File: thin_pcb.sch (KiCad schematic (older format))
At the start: 149 parts, among them J01 Conn_01x02, J02 Conn_01x02, J04 Conn_01x02, J06 Conn_01x02, J07 Conn_01x02, J08 Conn_01x02, J1 USB_B_Micro, J11 Conn_01x03, J12 Conn_01x03, J13 Conn_01x03, J14 Conn_01x03, J15 Conn_01x03, J16 Conn_01x03, J17 Conn_01x03, J18 Conn_01x03, J2 AudioJack4_Ground, J21 Conn_01x07, J22 Conn_01x07, J23 Conn_01x07, J24 Conn_01x07, J25 Conn_01x07, J26 Conn_01x07, J27 Conn_01x07, J28 Conn_01x07, J3 AudioJack4_Ground, J31 Conn_01x07, J32 Conn_01x07, J33 Conn_01x07, J34 Conn_01x07, J35 Conn_01x07, J36 Conn_01x07, J37 Conn_01x07, J38 Conn_01x07, J4 Conn_01x06, J41 Conn_01x04, J42 Conn_01x04, J43 Conn_01x04, J44 Conn_01x04, J45 Conn_01x04, J46 Conn_01x04, J47 Conn_01x04, J48 Conn_01x04, J5 Conn_01x06, J51 Conn_01x01, J52 Conn_01x01, J53 Conn_01x01, J54 Conn_01x01, J55 Conn_01x01, J56 Conn_01x01, J57 Conn_01x01, J58 Conn_01x01, J6 Conn_02x02, J7 Conn_01x02, SW11 SW_Push, SW12 SW_Push, SW13 SW_Push, SW14 SW_Push, SW15 SW_Push, SW21 SW_Push, SW22 SW_Push, SW23 SW_Push, SW24 SW_Push, SW25 SW_Push, SW252 SW_Push, SW31 SW_Push, SW32 SW_Push, SW33 SW_Push, SW34 SW_Push, SW35 SW_Push, SW41 SW_Push, SW42 SW_Push, SW422 SW_Push, SW43 SW_Push, SW44 SW_Push, SW45 SW_Push, SW452 SW_Push, SW51 SW_Push, SW52 SW_Push, SW522 SW_Push, SW53 SW_Push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

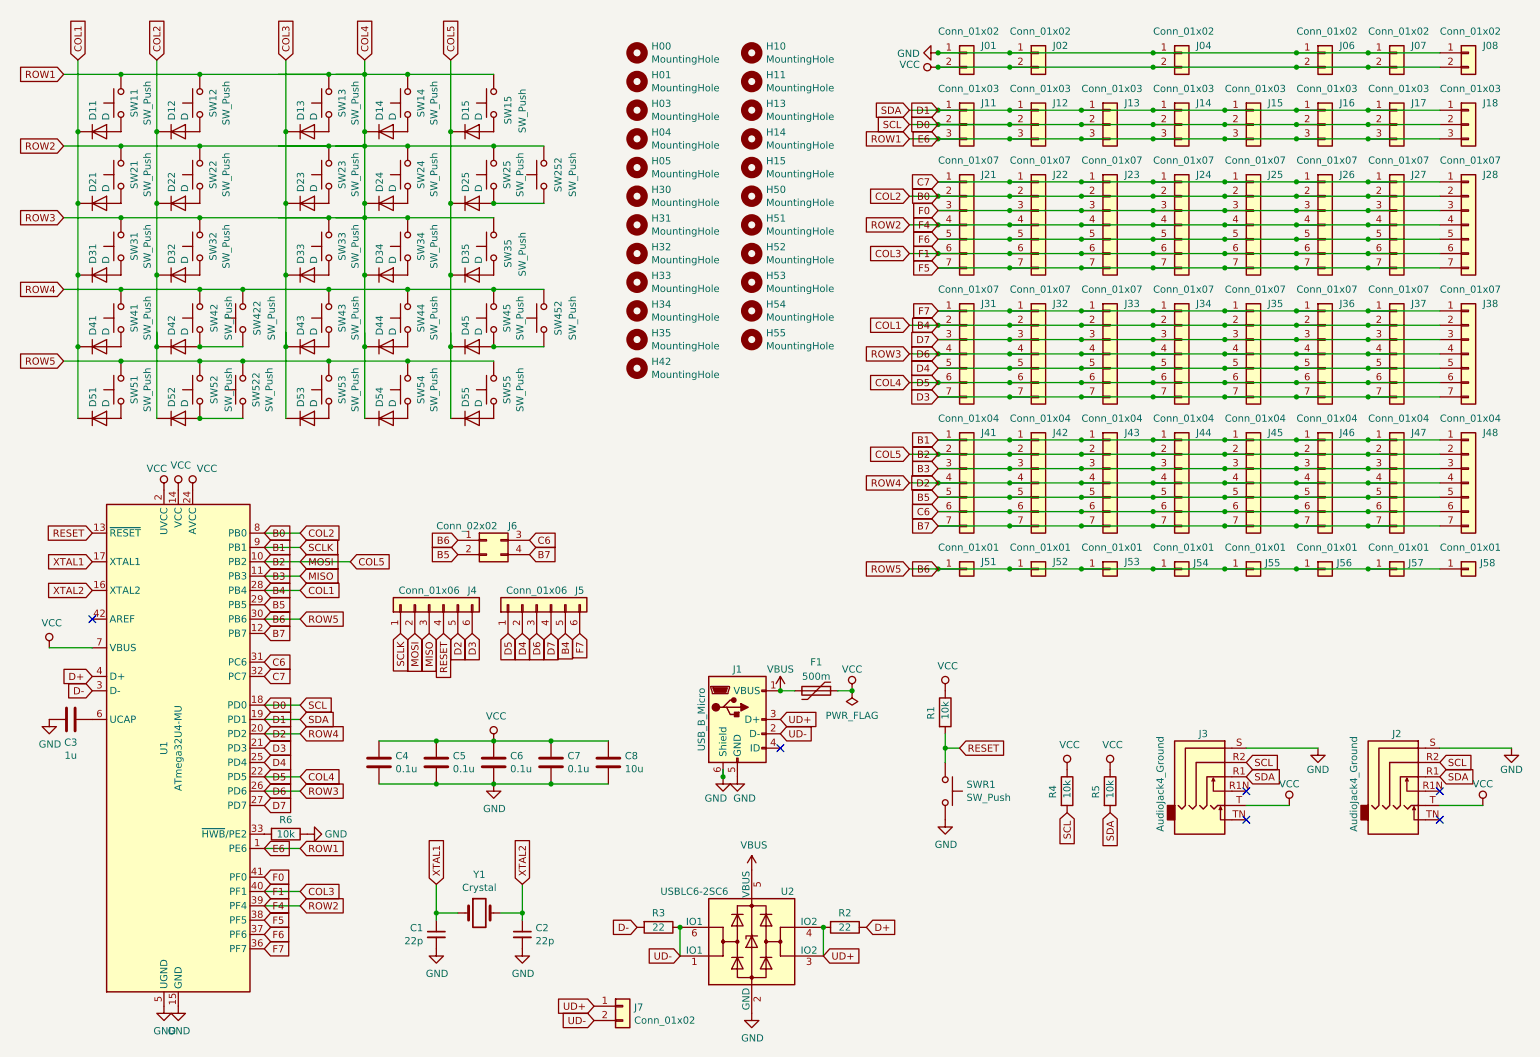
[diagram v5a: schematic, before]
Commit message: fix circuits labels
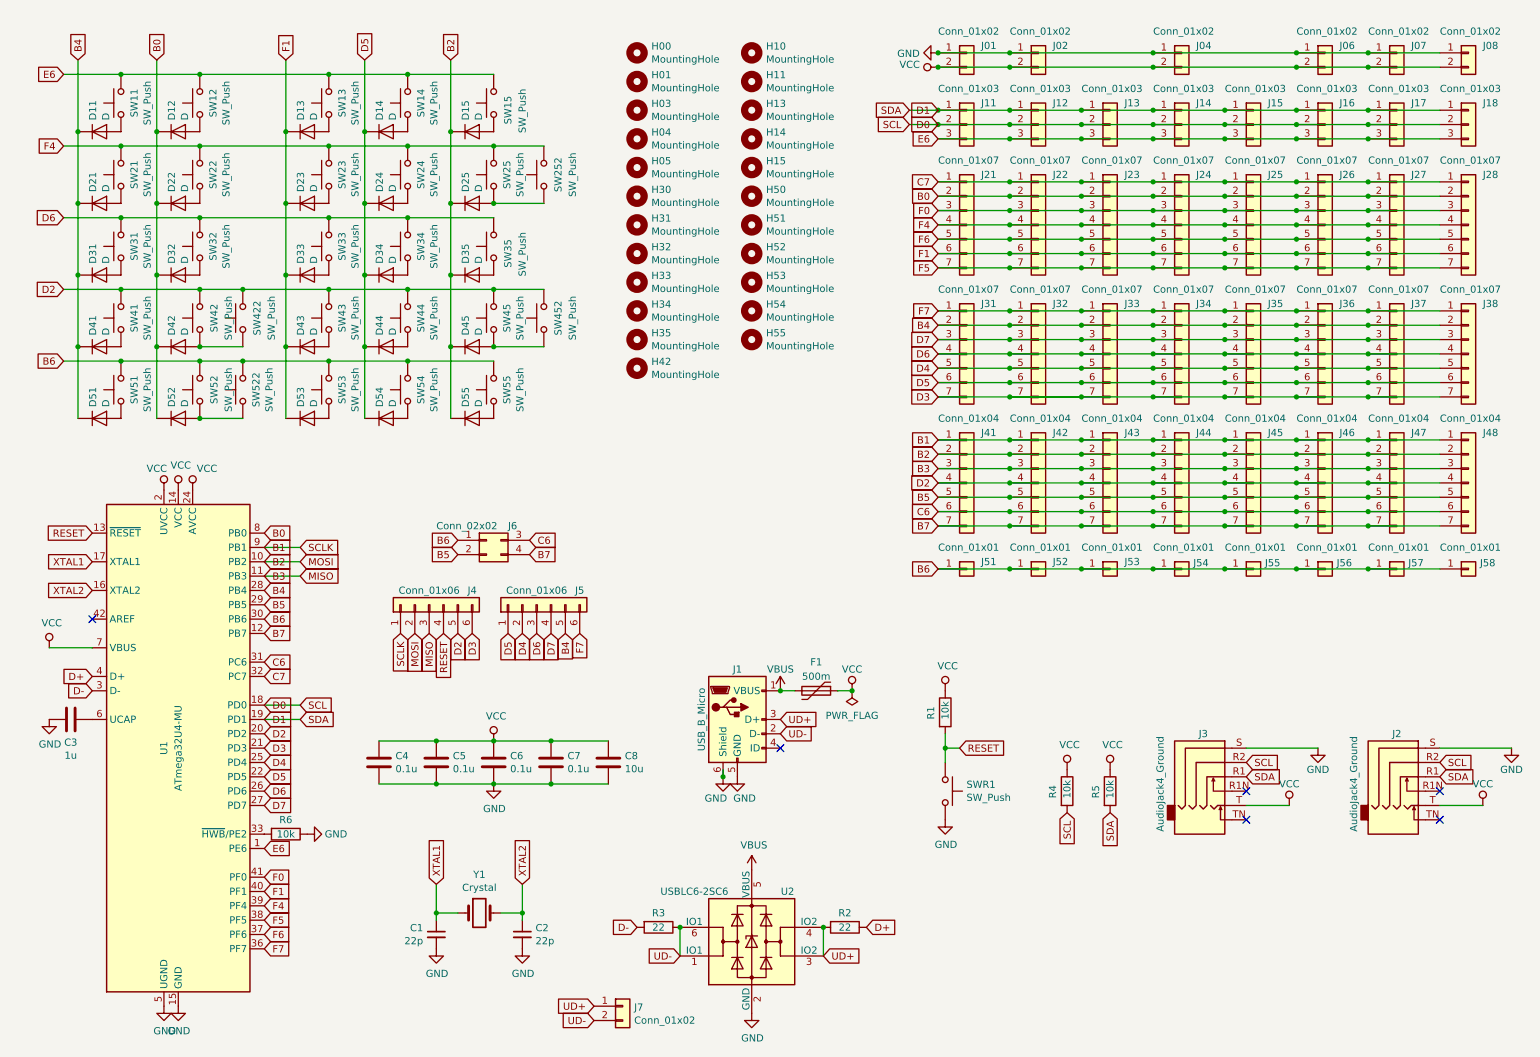
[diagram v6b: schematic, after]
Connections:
- net labels removed: COL1, COL2, COL3, COL4, COL5, ROW1, ROW2, ROW3, ROW4, ROW5
- wire segments 313 -> 281
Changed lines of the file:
@@
 	1    0    0    -1
 $EndComp
-Text GLabel 900  800  1    50   Input ~ 0
-COL1
-Text GLabel 1450 800  1    50   Input ~ 0
-COL2
-Text GLabel 800  900  0    50   Input ~ 0
-ROW1
-Text GLabel 800  1400 0    50   Input ~ 0
-ROW2
 $Comp
 L Switch:SW_Push SW22
@@
 	1    0    0    -1
 $EndComp
-Text GLabel 2350 800  1    50   Input ~ 0
-COL3
-Text GLabel 2900 800  1    50   Input ~ 0
-COL4
 $Comp
 L Switch:SW_Push SW24
@@
 	1    0    0    -1
 $EndComp
-Text GLabel 3500 800  1    50   Input ~ 0
-COL5
 $Comp
 L Switch:SW_Push SW25
@@
 	1    0    0    -1
 $EndComp
-Text GLabel 800  1900 0    50   Input ~ 0
-ROW3
-Text GLabel 800  2400 0    50   Input ~ 0
-ROW4
 $Comp
 L Switch:SW_Push SW42
@@
 	1    0    0    -1
 $EndComp
-Text GLabel 800  2900 0    50   Input ~ 0
-ROW5
 $Comp
 L Switch:SW_Push SW52
@@
 	0    -1   -1   0
 $EndComp
-Text GLabel 2450 4500 2    50   Input ~ 0
-COL1
-Text GLabel 2450 4100 2    50   Input ~ 0
-COL2
-Text GLabel 2450 6600 2    50   Input ~ 0
-COL3
-Text GLabel 2450 5800 2    50   Input ~ 0
-COL4
-Text GLabel 2800 4300 2    50   Input ~ 0
-COL5
-Text GLabel 2450 6300 2    50   Input ~ 0
-ROW1
-Text GLabel 2450 6700 2    50   Input ~ 0
-ROW2
-Text GLabel 2450 5900 2    50   Input ~ 0
-ROW3
-Text GLabel 2450 5500 2    50   Input ~ 0
-ROW4
-Text GLabel 2450 4700 2    50   Input ~ 0
-ROW5
 Text GLabel 2200 4100 2    50   Input ~ 0
 B0
@@
 Text GLabel 2200 5500 2    50   Input ~ 0
 D2
-Wire Wire Line
-	2200 6600 2450 6600
-Wire Wire Line
-	2200 4100 2450 4100
-Wire Wire Line
-	2200 4500 2450 4500
-Wire Wire Line
-	2200 5800 2450 5800
 Text GLabel 2200 5600 2    50   Input ~ 0
 D3
@@
 Text GLabel 2200 7000 2    50   Input ~ 0
 F7
-Wire Wire Line
-	2200 6300 2450 6300
-Wire Wire Line
-	2200 6700 2450 6700
-Wire Wire Line
-	2200 5900 2450 5900
-Wire Wire Line
-	2200 5500 2450 5500
-Wire Wire Line
-	2200 4700 2450 4700
 $Comp
 L power:VBUS #PWR0107
@@
 	5100 7050 5100 6850
 Connection ~ 5100 6850
-Text GLabel 6700 4350 0    50   Input ~ 0
-ROW5
-Text GLabel 6700 3750 0    50   Input ~ 0
-ROW4
-Text GLabel 6700 2850 0    50   Input ~ 0
-ROW3
-Text GLabel 6700 3050 0    50   Input ~ 0
-COL4
-Text GLabel 6700 3550 0    50   Input ~ 0
-COL5
 Connection ~ 900  1300
 Connection ~ 1200 900
@@
 	2350 800  2350 1300
 Wire Wire Line
-	2900 800  2900 900
-Wire Wire Line
 	3500 800  3500 1300
 Wire Wire Line
@@
 	2350 1800 2350 2300
 Wire Wire Line
-	2900 1800 2900 1900
-Wire Wire Line
 	3500 1800 3500 2300
 Wire Wire Line
@@
 Wire Wire Line
 	1450 1300 1450 1800
-Wire Wire Line
-	2900 1300 2900 1400
 Wire Wire Line
 	3500 1300 3500 1800
@@
 Connection ~ 2650 1400
 Connection ~ 2650 1900
-Connection ~ 2900 900
 Wire Wire Line
 	2900 900  3200 900
 Wire Wire Line
-	2900 900  2900 1300
-Connection ~ 2900 1400
-Wire Wire Line
 	2900 1400 3200 1400
 Wire Wire Line
-	2900 1400 2900 1800
-Connection ~ 2900 1900
-Wire Wire Line
 	2900 1900 3200 1900
-Wire Wire Line
-	2900 1900 2900 2300
 Wire Wire Line
 	1200 900  1750 900
@@
 Connection ~ 1750 3300
 Wire Wire Line
-	1450 2700 1450 2800
-Wire Wire Line
-	2300 900  2650 900
-Wire Wire Line
-	2300 1400 2650 1400
-Wire Wire Line
-	2300 1900 2650 1900
-Wire Wire Line
-	2350 2700 2350 2800
-Wire Wire Line
-	2700 900  2900 900
-Wire Wire Line
-	2700 1400 2900 1400
-Wire Wire Line
-	2700 1900 2900 1900
-Wire Wire Line
-	2900 2700 2900 2800
-Wire Wire Line
-	3500 2700 3500 2800
-Wire Wire Line
 	1450 2300 1450 2800
 Wire Wire Line
@@
 	9900 2250 10400 2250
 Wire Wire Line
-	6900 2550 7400 2550
-Connection ~ 7400 2550
-Wire Wire Line
 	7400 2550 7900 2550
 Connection ~ 7900 2550
@@
 	9900 2550 10400 2550
 Wire Wire Line
-	6900 2650 7400 2650
-Connection ~ 7400 2650
-Wire Wire Line
 	7400 2650 7900 2650
 Connection ~ 7900 2650
@@
 	9900 2650 10400 2650
 Wire Wire Line
-	6900 2750 7400 2750
-Connection ~ 7400 2750
-Wire Wire Line
 	7400 2750 7900 2750
 Connection ~ 7900 2750
@@
 	9900 2750 10400 2750
 Wire Wire Line
-	6900 2850 7400 2850
-Connection ~ 7400 2850
-Wire Wire Line
 	7400 2850 7900 2850
 Connection ~ 7900 2850
@@
 	9900 2850 10400 2850
 Wire Wire Line
-	6900 2950 7400 2950
-Connection ~ 7400 2950
-Wire Wire Line
 	7400 2950 7900 2950
 Connection ~ 7900 2950
@@
 	9900 2950 10400 2950
 Wire Wire Line
-	6900 3050 7400 3050
-Connection ~ 7400 3050
-Wire Wire Line
 	7400 3050 7900 3050
 Connection ~ 7900 3050
@@
 Wire Wire Line
 	9900 3050 10400 3050
-Wire Wire Line
-	6900 3150 7400 3150
-Connection ~ 7400 3150
 Wire Wire Line
 	7400 3150 7900 3150
@@
 Text GLabel 6900 2650 0    50   Input ~ 0
 B4
-Text GLabel 6700 2650 0    50   Input ~ 0
-COL1
-Text GLabel 6700 1750 0    50   Input ~ 0
-COL2
-Text GLabel 6700 2150 0    50   Input ~ 0
-COL3
-Text GLabel 6700 1350 0    50   Input ~ 0
-ROW1
-Text GLabel 6700 1950 0    50   Input ~ 0
-ROW2
 Text GLabel 6900 4350 0    50   Input ~ 0
 B6
@@
 Text GLabel 2200 4400 2    50   Input ~ 0
 B3
-Wire Wire Line
-	2200 4300 2800 4300
 Text GLabel 2200 5300 2    50   Input ~ 0
 D0
@@
 Text GLabel 6900 3750 0    50   Input ~ 0
 D2
-Wire Wire Line
-	6700 3550 6900 3550
-Connection ~ 6900 3550
-Wire Wire Line
-	6700 3750 6900 3750
-Connection ~ 6900 3750
 Text GLabel 6900 2850 0    50   Input ~ 0
 D6
@@
 Text GLabel 6900 3650 0    50   Input ~ 0
 B3
-Wire Wire Line
-	6700 2650 6900 2650
-Connection ~ 6900 2650
-Wire Wire Line
-	6700 2850 6900 2850
-Connection ~ 6900 2850
-Wire Wire Line
-	6700 3050 6900 3050
-Connection ~ 6900 3050
-Wire Wire Line
-	6700 2150 6900 2150
-Connection ~ 6900 2150
-Wire Wire Line
-	6700 1950 6900 1950
-Connection ~ 6900 1950
-Wire Wire Line
-	6700 1750 6900 1750
-Connection ~ 6900 1750
-Wire Wire Line
-	6700 4350 6900 4350
-Connection ~ 6900 4350
-Wire Wire Line
-	6700 1350 6900 1350
-Connection ~ 6900 1350
 Text GLabel 6900 1150 0    50   Input ~ 0
 D1
@@
 Connection ~ 6900 1250
 Wire Wire Line
-	6900 1250 7400 1250
+	2900 800  2900 1300
+Wire Wire Line
+	2900 1300 2900 1800
+Wire Wire Line
+	2900 1800 2900 2300
+Text GLabel 800  900  0    50   Input ~ 0
+E6
+Text GLabel 800  1400 0    50   Input ~ 0
+F4
+Text GLabel 800  1900 0    50   Input ~ 0
+D6
+Text GLabel 800  2400 0    50   Input ~ 0
+D2
+Text GLabel 800  2900 0    50   Input ~ 0
+B6
+Text GLabel 900  800  1    50   Input ~ 0
+B4
+Text GLabel 1450 800  1    50   Input ~ 0
+B0
+Text GLabel 2350 800  1    50   Input ~ 0
+F1
+Text GLabel 2900 800  1    50   Input ~ 0
+D5
+Text GLabel 3500 800  1    50   Input ~ 0
+B2
+Wire Wire Line
+	2200 4300 2450 4300
+Wire Wire Line
+	6900 2550 7400 2550
+Connection ~ 7400 2550
+Wire Wire Line
+	6900 2650 7400 2650
+Connection ~ 7400 2650
+Wire Wire Line
+	6900 2750 7400 2750
+Connection ~ 7400 2750
+Wire Wire Line
+	6900 2850 7400 2850
+Connection ~ 7400 2850
+Connection ~ 7400 2950
+Wire Wire Line
+	7400 2950 6900 2950
+Wire Wire Line
+	6900 3050 7400 3050
+Connection ~ 7400 3050
+Wire Wire Line
+	7900 3150 7400 3150
+Connection ~ 7400 3150
+Wire Wire Line
+	7400 3150 6900 3150
 $EndSCHEMATC

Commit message: reset pinhole
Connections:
- net B1: now also J4.2 (Pin_2); no longer J4.1 (Pin_1)
- net B2: now also J4.3 (Pin_3); no longer J4.2 (Pin_2)
- net B3: now also J4.4 (Pin_4); no longer J4.3 (Pin_3)
- net RESET: now also J4.1 (Pin_1); no longer J4.4 (Pin_4)
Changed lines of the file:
@@
 Text GLabel 9050 5700 2    50   Input ~ 0
 SCL
+Text GLabel 3450 4800 3    50   Input ~ 0
+MISO
 Text GLabel 3350 4800 3    50   Input ~ 0
-MISO
+MOSI
 Text GLabel 3250 4800 3    50   Input ~ 0
-MOSI
+SCLK
 Text GLabel 3150 4800 3    50   Input ~ 0
-SCLK
-Text GLabel 3450 4800 3    50   Input ~ 0
 RESET
 $Comp
@@
 	6900 3050 7400 3050
 Connection ~ 7400 3050
-Wire Wire Line
-	7900 3150 7400 3150
 Connection ~ 7400 3150
 Wire Wire Line

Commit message: breaklines
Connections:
- net B1: now also J41.3 (Pin_3), J42.3 (Pin_3), J43.3 (Pin_3), J44.3 (Pin_3), J45.3 (Pin_3), J46.3 (Pin_3), J47.3 (Pin_3), J48.3 (Pin_3); no longer J41.1 (Pin_1), J42.1 (Pin_1), J43.1 (Pin_1), J44.1 (Pin_1), J45.1 (Pin_1), J46.1 (Pin_1), J47.1 (Pin_1), J48.1 (Pin_1)
- net B3: now also J41.1 (Pin_1), J42.1 (Pin_1), J43.1 (Pin_1), J44.1 (Pin_1), J45.1 (Pin_1), J46.1 (Pin_1), J47.1 (Pin_1), J48.1 (Pin_1); no longer J41.3 (Pin_3), J42.3 (Pin_3), J43.3 (Pin_3), J44.3 (Pin_3), J45.3 (Pin_3), J46.3 (Pin_3), J47.3 (Pin_3), J48.3 (Pin_3)
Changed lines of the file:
@@
 Text GLabel 6900 3550 0    50   Input ~ 0
 B2
-Text GLabel 6900 3450 0    50   Input ~ 0
+Text GLabel 6900 3650 0    50   Input ~ 0
 B1
 Text GLabel 6900 3750 0    50   Input ~ 0
@@
 Text GLabel 6900 3050 0    50   Input ~ 0
 D5
-Text GLabel 6900 3650 0    50   Input ~ 0
+Text GLabel 6900 3450 0    50   Input ~ 0
 B3
 Text GLabel 6900 1150 0    50   Input ~ 0
